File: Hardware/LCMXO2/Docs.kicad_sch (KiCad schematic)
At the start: 0 parts

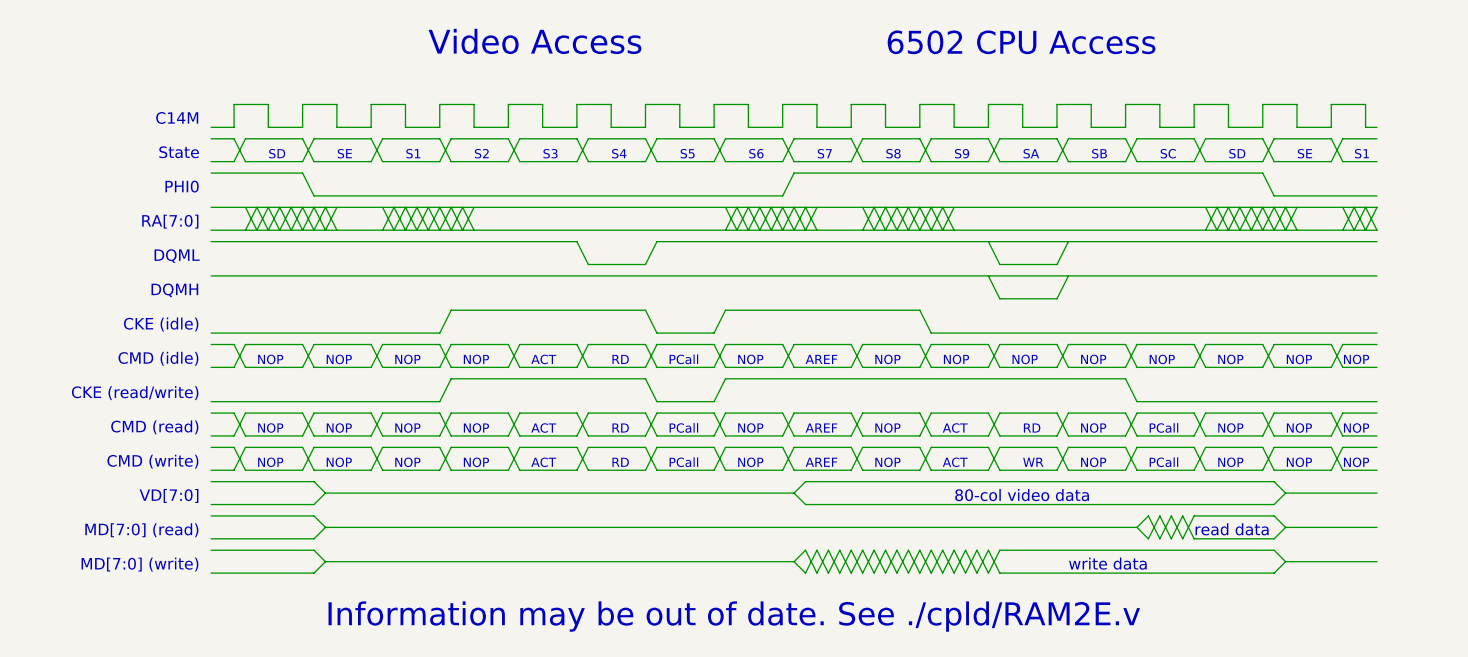
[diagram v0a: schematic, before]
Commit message: Revert "As sent to testers"
This reverts commit 4249ebe98332ad6fb679362fa153720a3e50f79b.
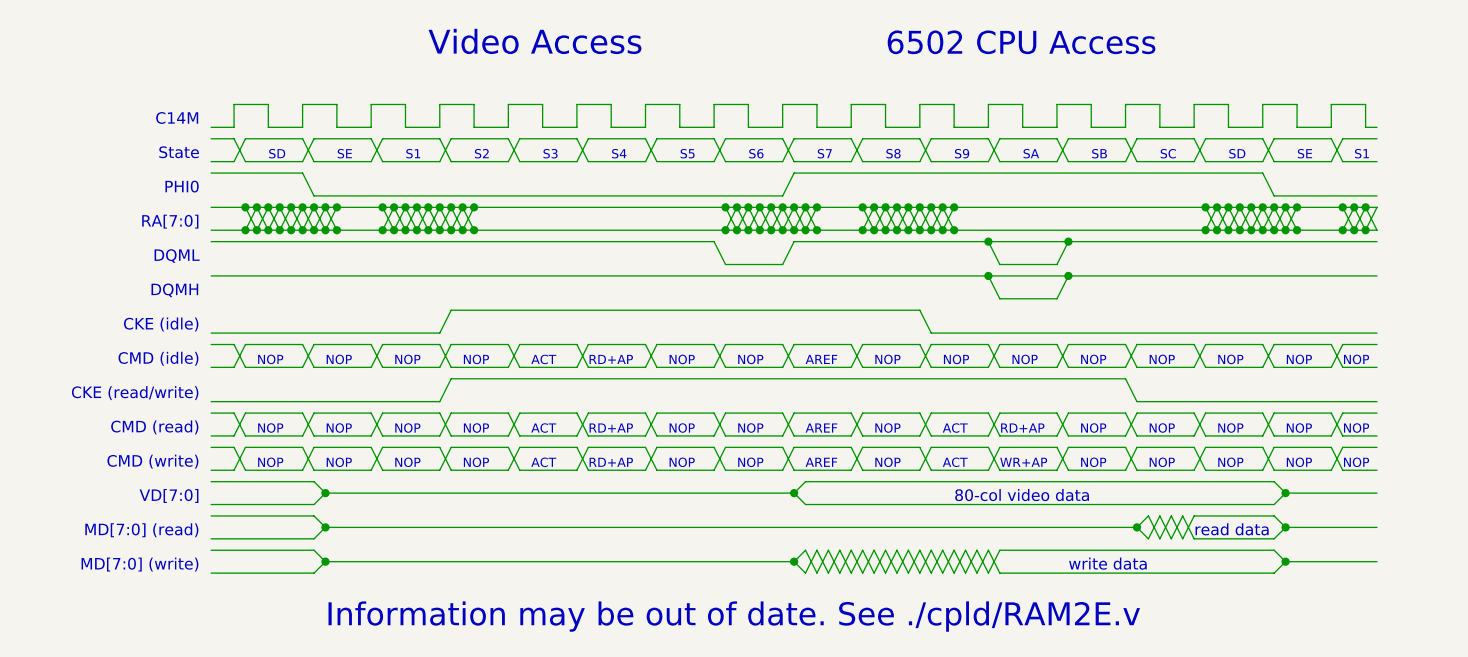
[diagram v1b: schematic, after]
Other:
- note added: "RD+AP"
- note added: "WR+AP"
- note removed: "PCall"
- note removed: "RD"
- note removed: "WR"

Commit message: As sent to testers
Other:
- note added: "PCall"
- note added: "RD"
- note added: "WR"
- note removed: "RD+AP"
- note removed: "WR+AP"
